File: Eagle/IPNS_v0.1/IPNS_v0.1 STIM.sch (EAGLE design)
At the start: 19 parts, among them J1 OUTPUT CONN, J2 POL SWITCH CONN, J3 LEFT CONN, J4 RIGHT CONN, U1 LTC3459ES6TRMPBF, U2 LT1492CS8TRPBF

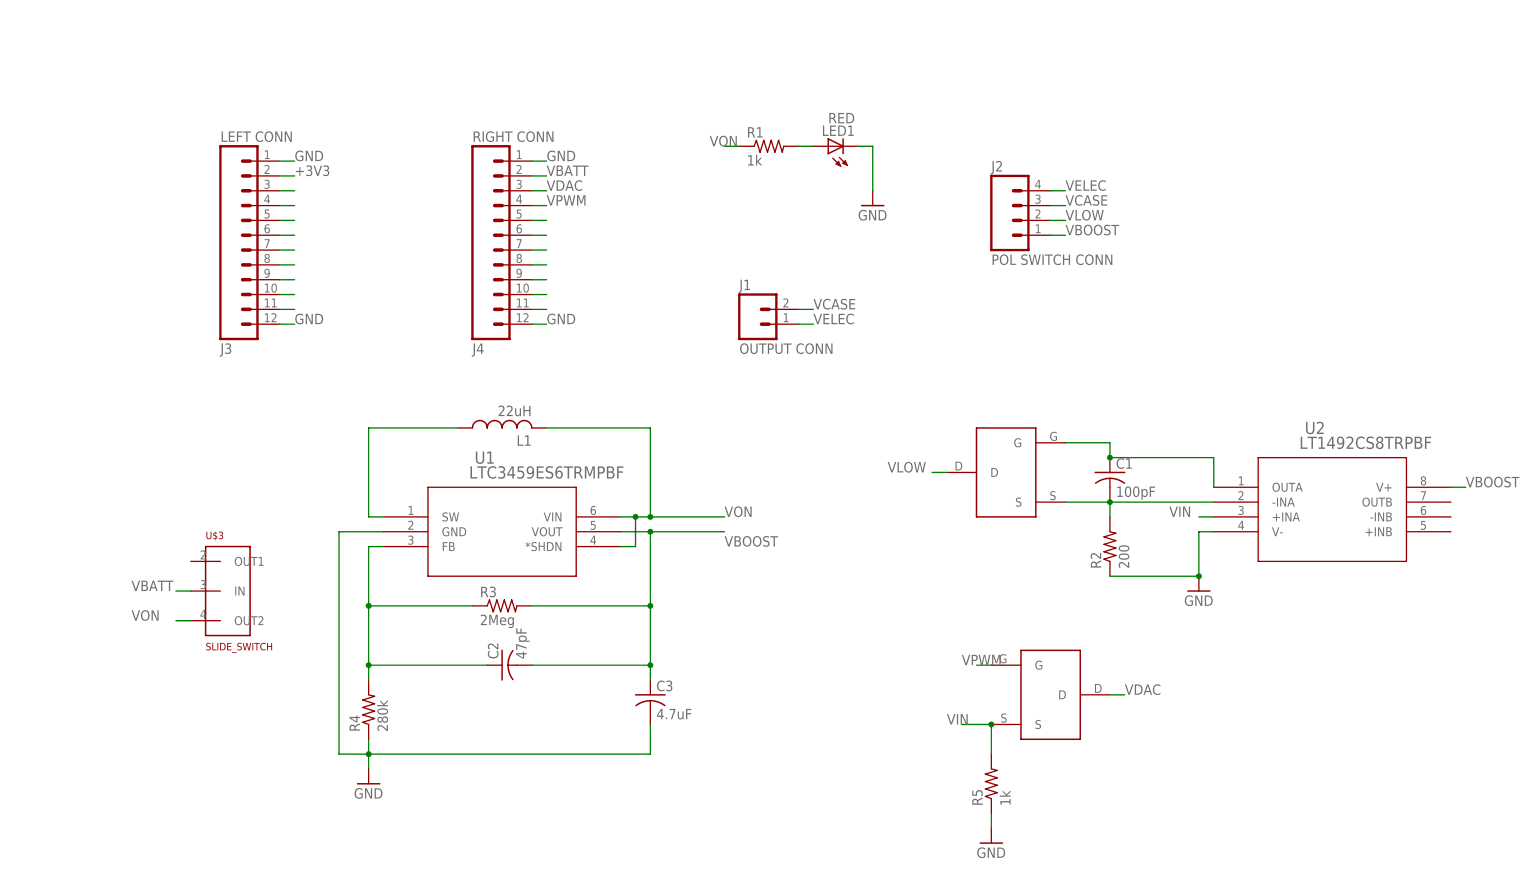
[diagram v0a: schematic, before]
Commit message: Routed everything; no DRC errors other than Stop Mask
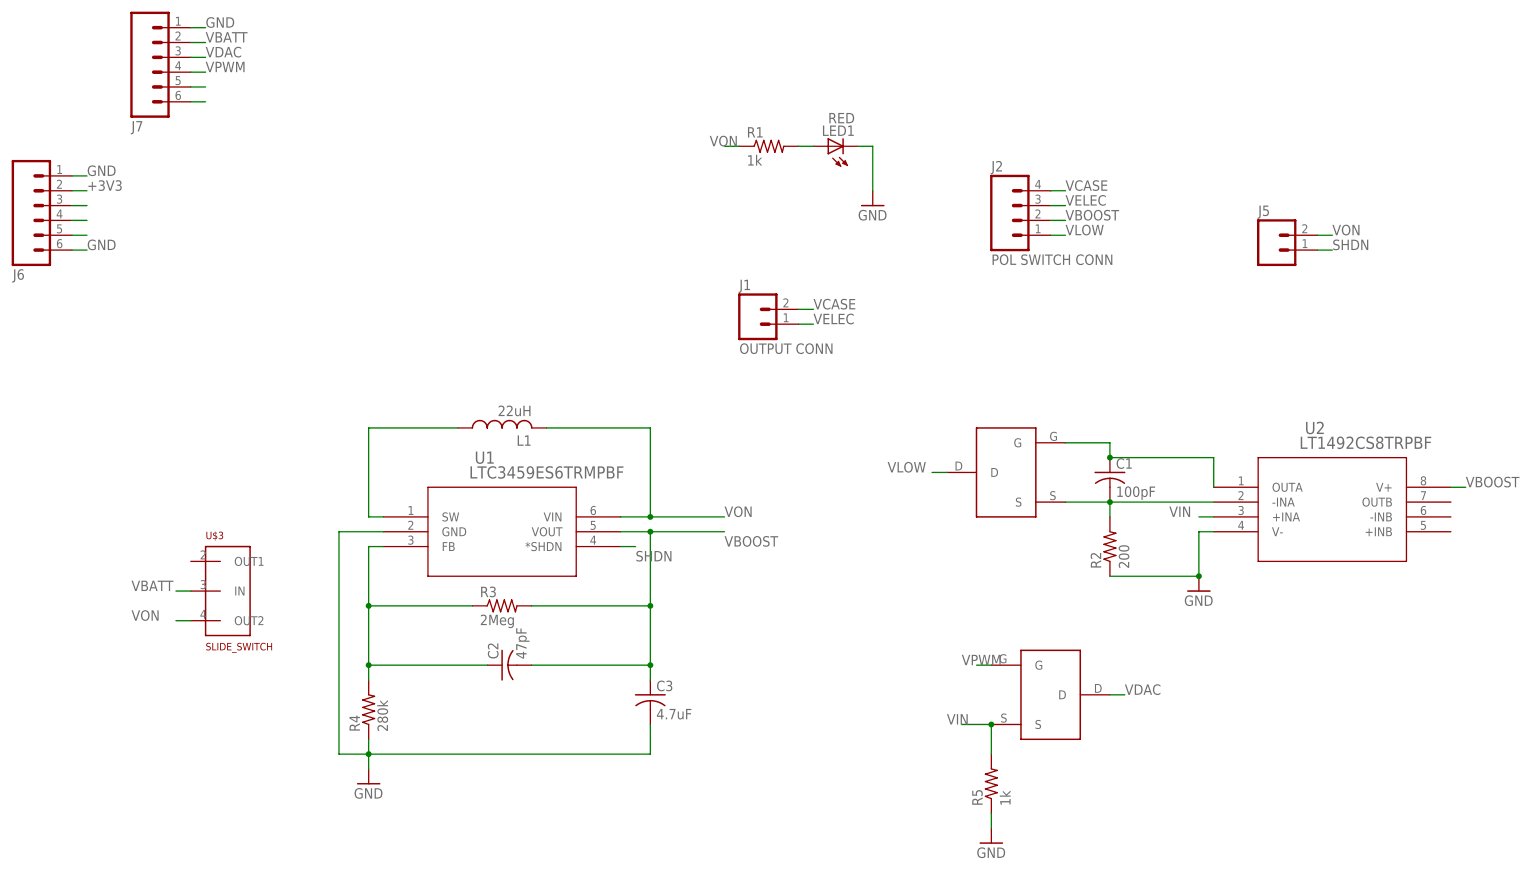
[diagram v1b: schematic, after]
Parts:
- removed J3: LEFT CONN, IPNS_Lib_v0.1:M12PTH
- removed J4: RIGHT CONN, IPNS_Lib_v0.1:M12PTH
- added J5: (no value), IPNS_Lib_v0.1:M02PTH
- added J6, J7: (no value), IPNS_Lib_v0.1:M06SILK_FEMALE_PTH
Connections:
- removed net N$10: J3.6
- removed net N$11: J3.7
- removed net N$12: J3.8
- removed net N$13: J3.9
- removed net N$14: J3.10
- removed net N$15: J3.11
- removed net N$18: J4.11
- removed net N$19: J4.10
- removed net N$20: J4.9
- removed net N$21: J4.8
- removed net N$22: J4.7
- removed net N$23: J4.6
- removed net N$24: J4.5
- removed net N$7: J3.3
- removed net N$8: J3.4
- removed net N$9: J3.5
- new net N$25: J6.5
- new net N$26: J6.4
- new net N$27: J6.3
- new net N$29: J7.5
- new net N$30: J7.6
- new net SHDN: J5.1, U1.*SHDN
- net +3V3: now also J6.2; no longer J3.2
- net GND: now also J6.1, J6.6, J7.1; no longer J3.1, J3.12, J4.1, J4.12
- net VBATT: now also J7.2; no longer J4.2
- net VBOOST: now also J2.2; no longer J2.1
- net VCASE: now also J2.4; no longer J2.3
- net VDAC: now also J7.3; no longer J4.3
- net VELEC: now also J2.3; no longer J2.4
- net VLOW: now also J2.1; no longer J2.2
- net VON: now also J5.2; no longer U1.*SHDN
- net VPWM: now also J7.4; no longer J4.4

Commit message: Broke out more pins on the MCU module
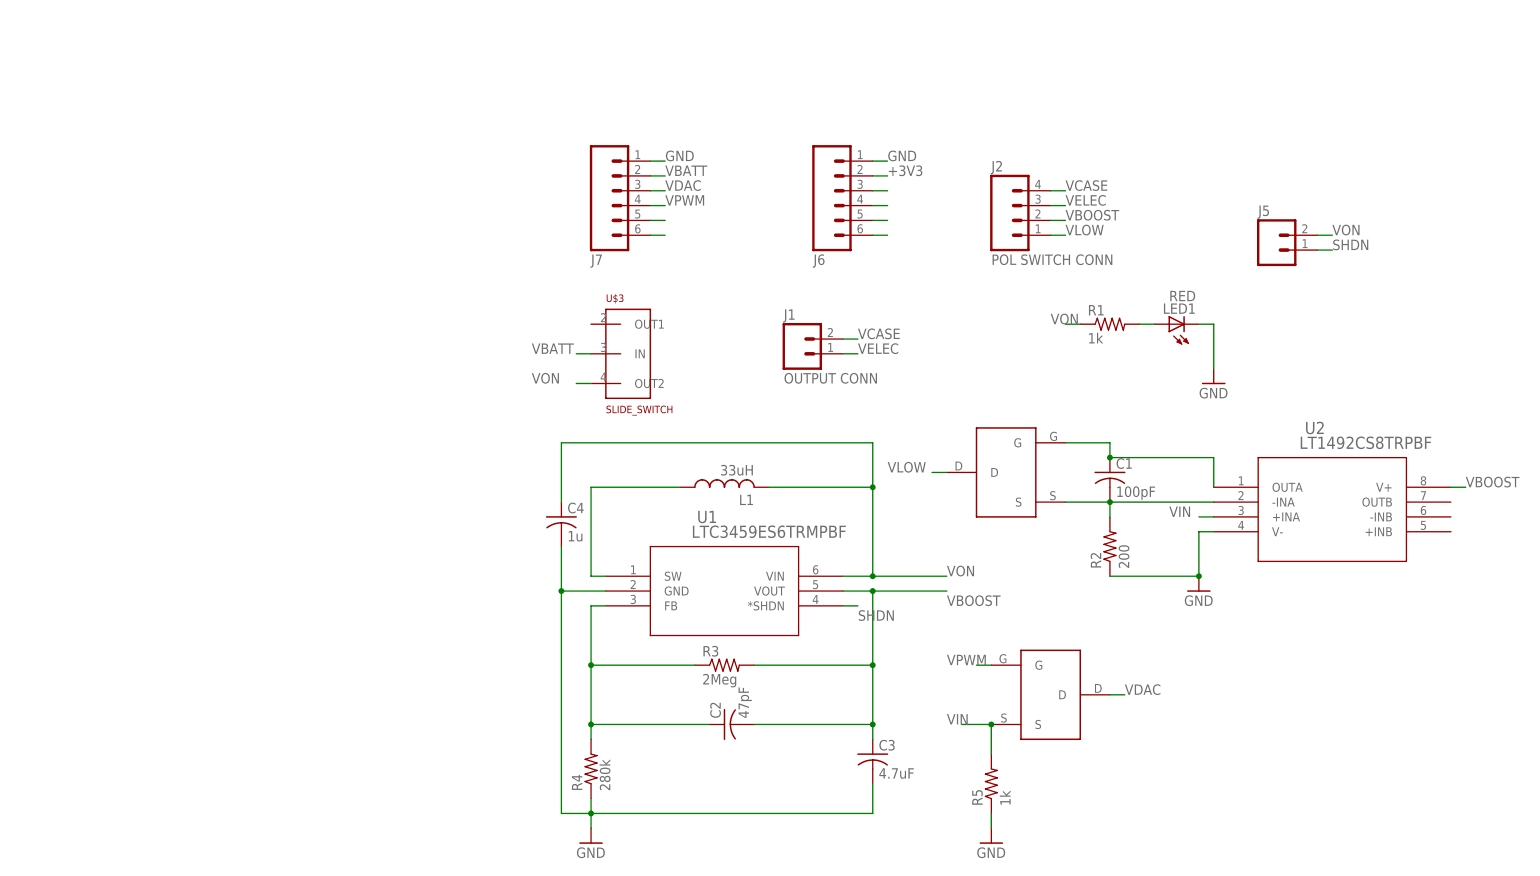
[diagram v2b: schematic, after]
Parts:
- added C4: 1u, IPNS_Lib_v0.1:C-USC0805
- L1: value 22uH -> 33uH
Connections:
- new net N$3: J6.6
- net GND: now also C4.2; no longer J6.6
- net VON: now also C4.1
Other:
- moved on the sheet: C2, C3, J1, J6, J7, L1, LED1, R1, R3, R4, U$3, U1
